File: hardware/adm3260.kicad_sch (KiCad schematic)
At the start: 18 parts, among them Q11 BS170, Q12 BSS84, Q3 BSS84, U4 ADM3260ARSZ

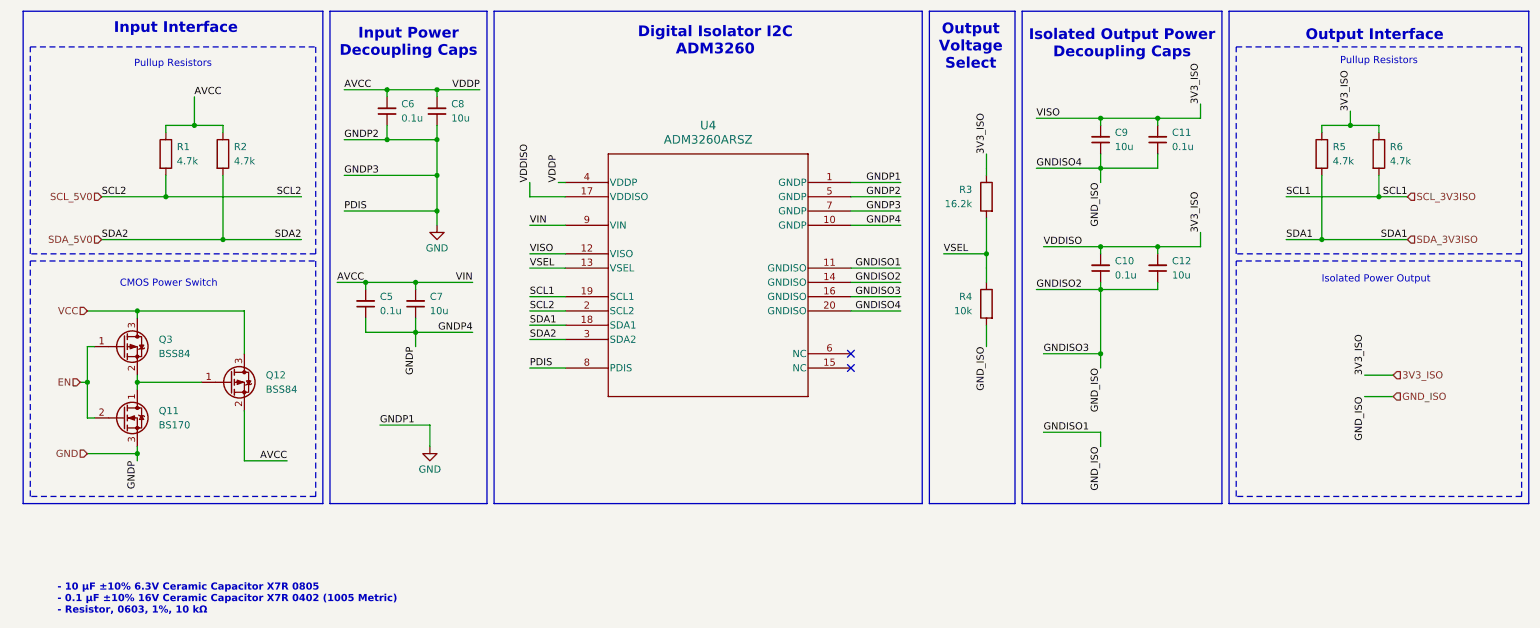
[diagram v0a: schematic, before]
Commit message: removed legacy folders
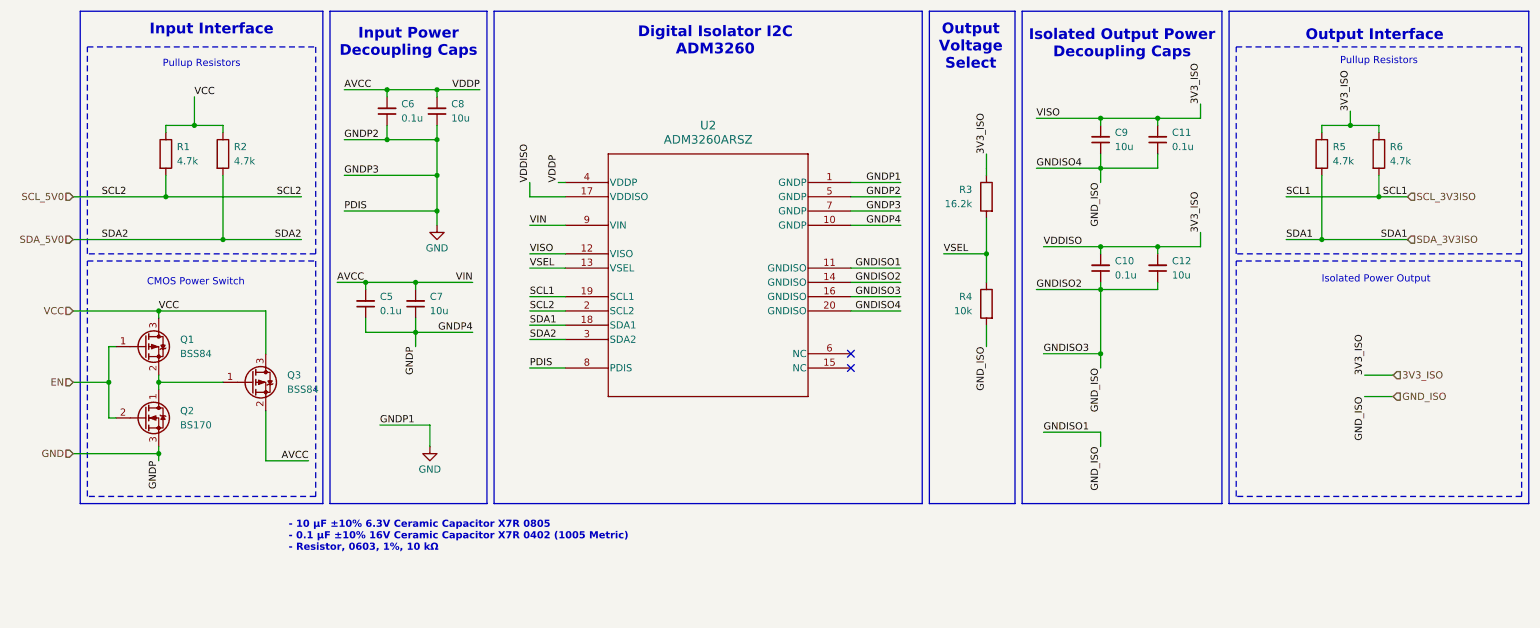
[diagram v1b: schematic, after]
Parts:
- C10, C11, C5, C6: footprint Capacitor_SMD:C_0402_1005Metric_Pad0.74x0.62mm_HandSolder -> Capacitor_SMD:C_0603_1608Metric_Pad1.08x0.95mm_HandSolder
- Q2: renamed from Q11; footprint Package_TO_SOT_THT:TO-92_Inline -> Package_TO_SOT_SMD:SOT-23
- renumbered Q3 to Q1, Q12 to Q3, U4 to U2
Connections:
- net AVCC: no longer R1.1, R2.1
- net VCC: now also R1.1, R2.1
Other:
- moved on the sheet: Q1, Q2, Q3
